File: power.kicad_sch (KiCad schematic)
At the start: 40 parts

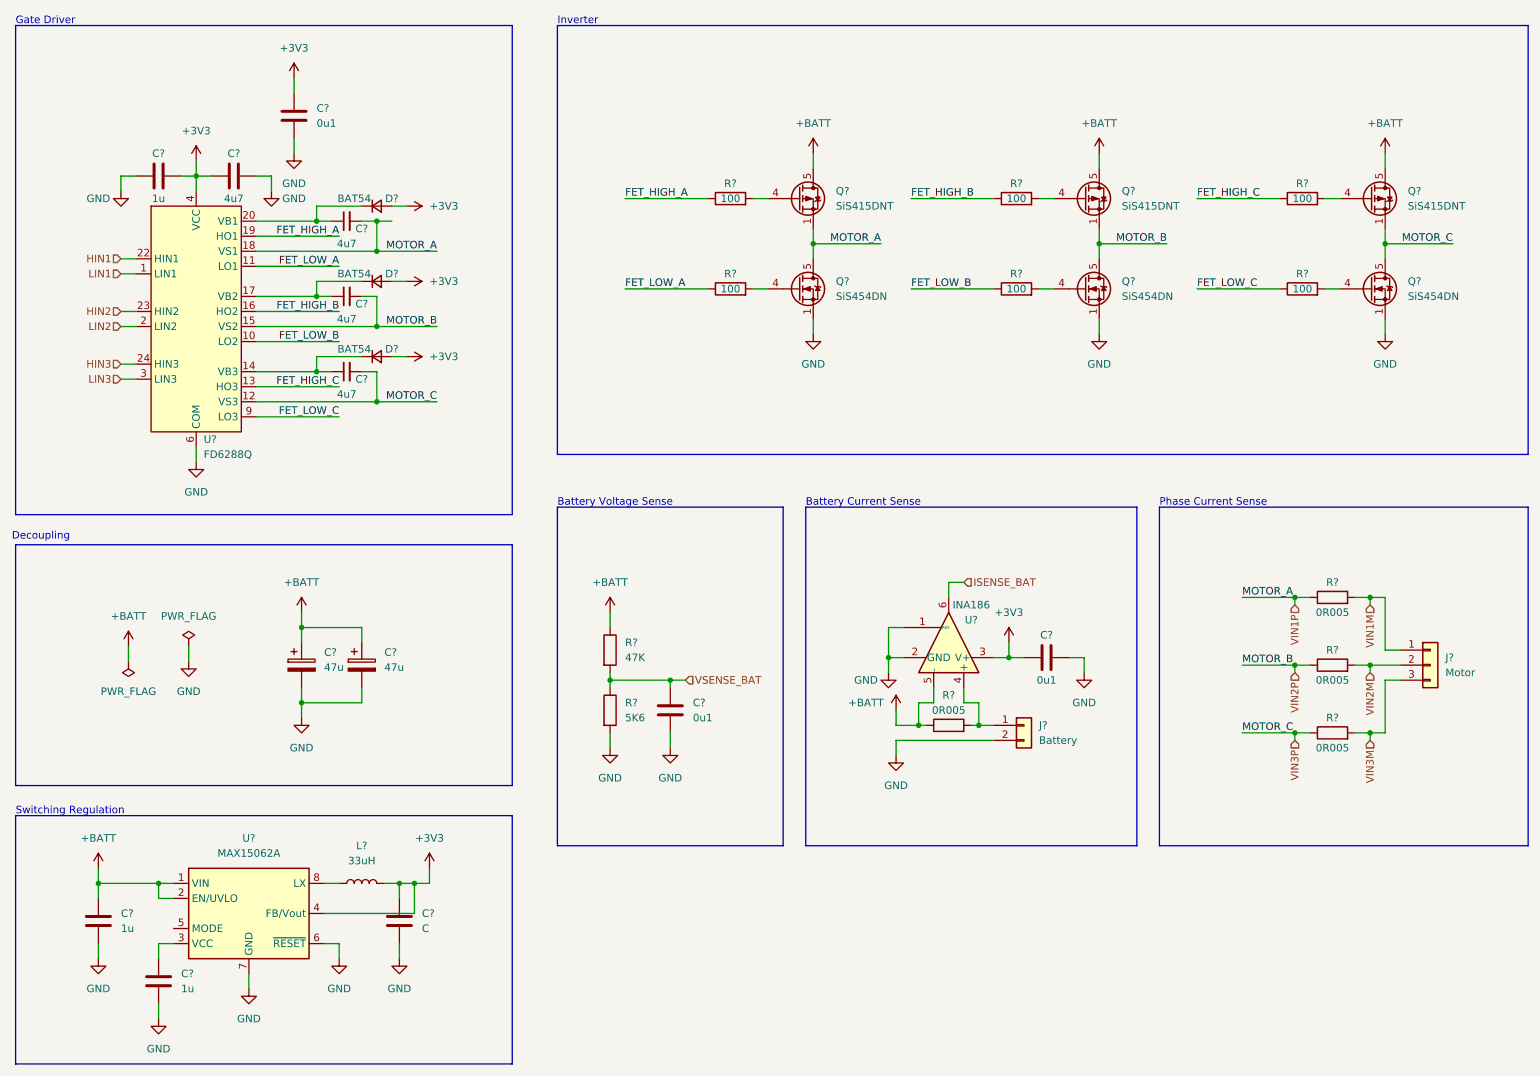
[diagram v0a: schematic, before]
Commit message: finish schematic draft, start layout
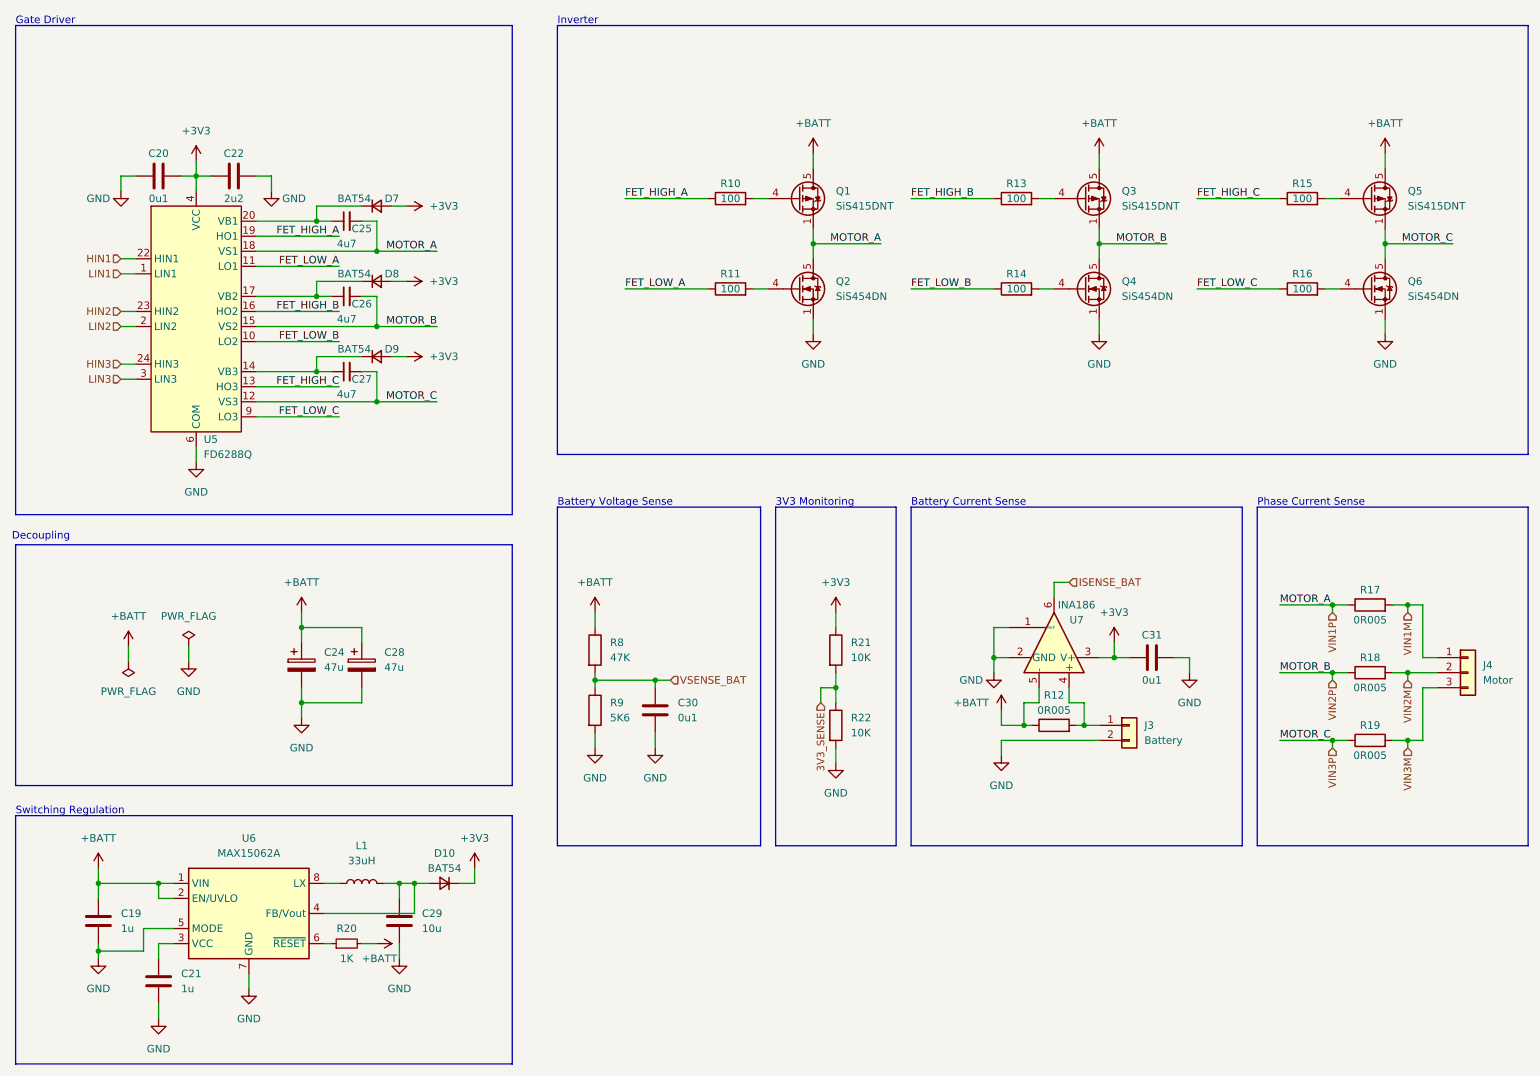
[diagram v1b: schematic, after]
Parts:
- removed C?: 0u1, symbol Device:C
- added D10: BAT54, Diode_SMD:D_SOD-523, symbol Device:D_Small
- added R20: 1K, Resistor_SMD:R_0402_1005Metric, symbol Device:R_Small
- added R21, R22: 10K, Resistor_SMD:R_0402_1005Metric, symbol Device:R
- C19: renamed from C?; footprint (none) -> Capacitor_SMD:C_0805_2012Metric
- C20: renamed from C?; value 1u -> 0u1; footprint (none) -> Capacitor_SMD:C_0402_1005Metric
- C21: renamed from C?; footprint (none) -> Capacitor_SMD:C_0603_1608Metric
- C22: renamed from C?; value 4u7 -> 2u2; footprint (none) -> Capacitor_SMD:C_0402_1005Metric
- C24, C28: renamed from C?; footprint (none) -> Capacitor_SMD:C_1206_3216Metric
- C25, C26, C27, C30, C31: renamed from C?; footprint (none) -> Capacitor_SMD:C_0402_1005Metric
- C29: renamed from C?; value C -> 10u; footprint (none) -> Capacitor_SMD:C_0603_1608Metric
- D7, D8, D9: renamed from D?; footprint (none) -> Diode_SMD:D_SOD-723
- J3: renamed from J?; footprint (none) -> Connector_Molex:Molex_Micro-Fit_3.0_43650-0200_1x02_P3.00mm_Horizontal
- J4: renamed from J?; footprint (none) -> Connector_Molex:Molex_Micro-Fit_3.0_43650-0300_1x03_P3.00mm_Horizontal
- L1: renamed from L?; footprint (none) -> Inductor_SMD:L_1210_3225Metric
- R10, R11, R13, R14, R15, R16, R8, R9: renamed from R?; footprint (none) -> Resistor_SMD:R_0402_1005Metric
- R12, R17, R18, R19: renamed from R?; footprint (none) -> Resistor_SMD:R_1210_3225Metric
- U5: renamed from U?; footprint (none) -> Package_DFN_QFN:QFN-24-1EP_4x4mm_P0.5mm_EP2.7x2.7mm
- gave numbers to parts that had none: 8
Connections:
- net +3V3: now also D10.1 (K), R21.1; no longer C29.1, L1.2, U6.4 (FB/Vout)
- net +BATT: now also R20.2
- net GND: now also U6.5 (MODE), R22.2; no longer U6.6 (~{RESET})
- new net: C29.1, D10.2 (A), L1.2, U6.4 (FB/Vout)
- new net: R20.1, U6.6 (~{RESET})
- new net 3V3_SENSE: R21.2, R22.1
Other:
- note added: "3V3 Monitoring"
- moved on the sheet: C30, C31, J3, J4, R12, R17, R18, R19, R8, R9, U7
